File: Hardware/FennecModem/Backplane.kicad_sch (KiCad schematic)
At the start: 28 parts, among them J1 SEL_ADDR, J3 EN_ADDR, J4 CARD_EN_BYPASS, Q901 MMBT3904, U2 SN74CBTLV3245A, U9 LM2596S-5

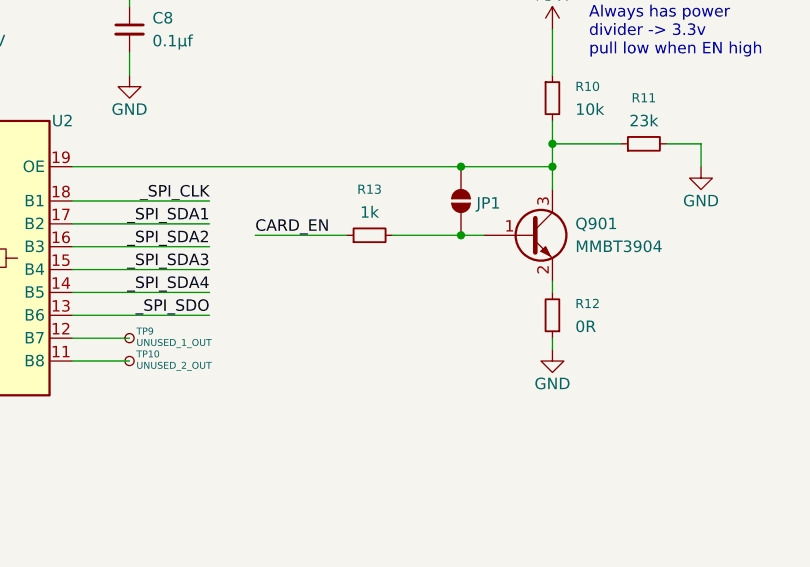
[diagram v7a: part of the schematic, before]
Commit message: Add CARD_EN note
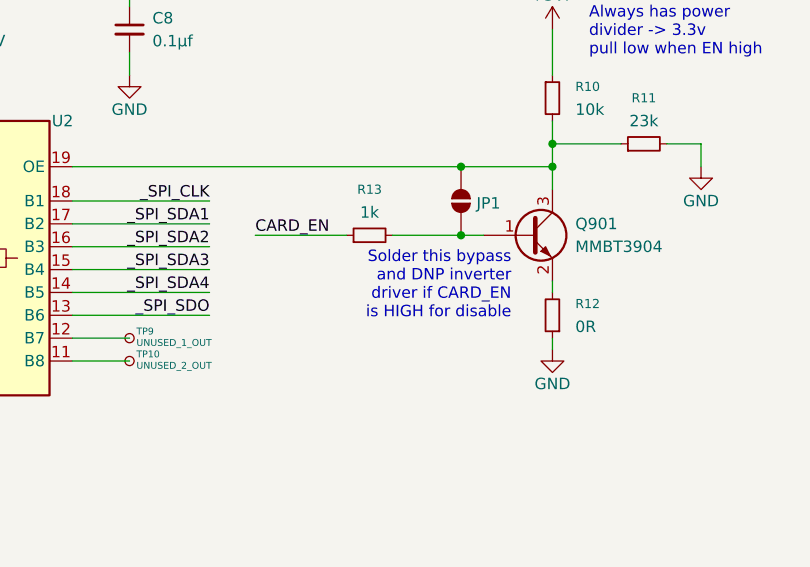
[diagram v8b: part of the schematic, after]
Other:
- note added: "Solder this bypass and DNP inverter driver if CARD_EN is HIGH for disable"
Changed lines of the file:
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@@
 	(generator_version "9.0")
 	(paper "A4")
+	(text "Solder this bypass\nand DNP inverter\ndriver if CARD_EN\nis HIGH for disable"
+		(exclude_from_sim no)
+		(at 199.898 74.168 0)
+		(effects
+			(font
+				(size 1.27 1.27)
+			)
+			(justify right top)
+		)
+	)
 	(text "5V/2kohm = 2.5mA"
 		(exclude_from_sim no)
